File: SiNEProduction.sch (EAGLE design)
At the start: 35 parts, among them IC1 74HCT164D, IC3 ATTINY24/44/84-SSU, J1 AVR_SPI_PRG_6NS

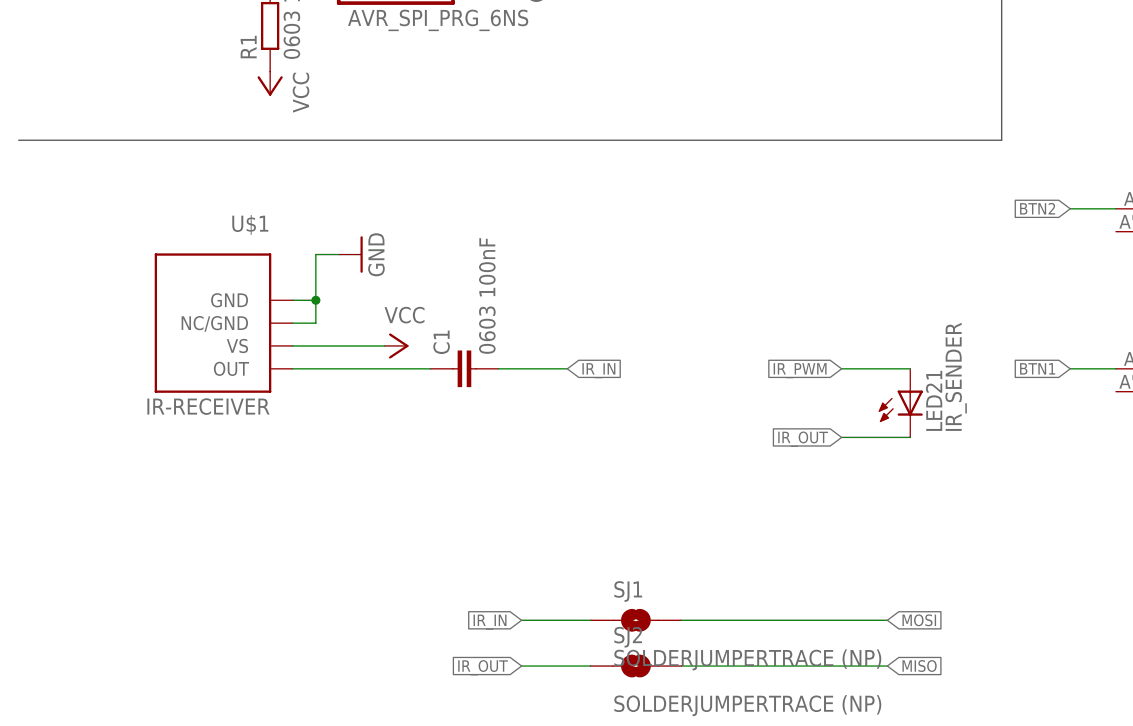
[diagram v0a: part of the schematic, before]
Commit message: Updated to use the combined IR Receiver footprint in case we have to switch parts
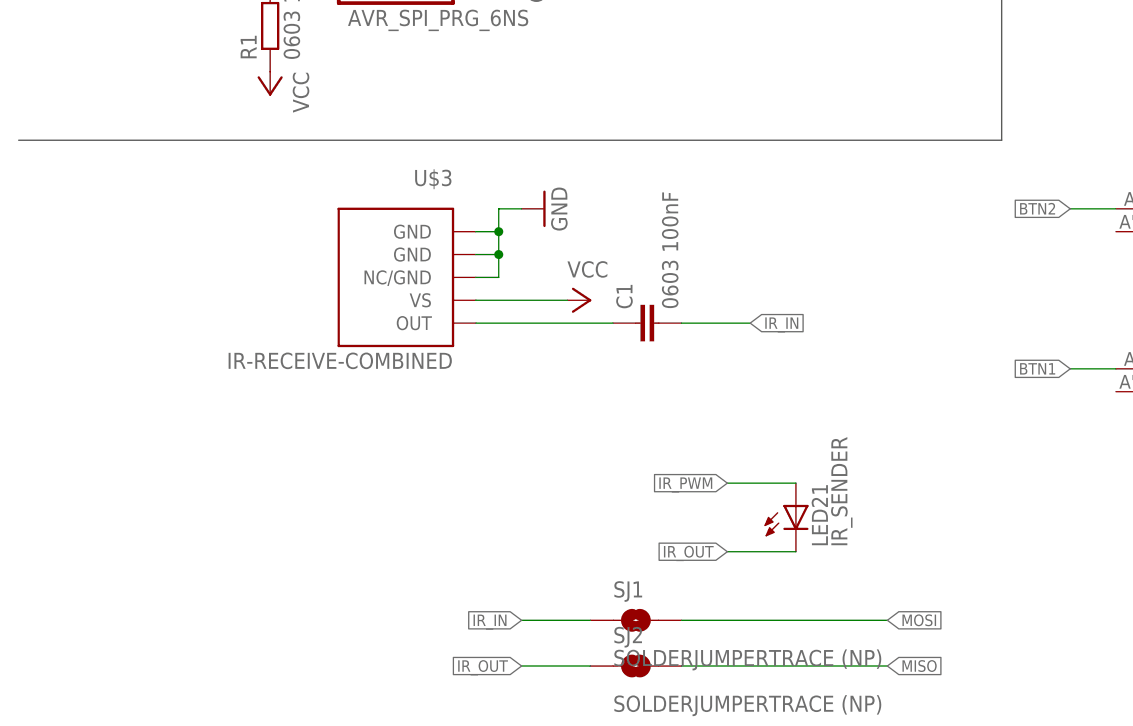
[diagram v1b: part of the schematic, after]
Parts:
- removed U$1: IR-RECEIVER, SiNE Parts:IR-RECEIVER
- added U$3: IR-RECEIVE-COMBINED, SiNE Parts:IR-RECEIVE-COMBINED
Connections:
- net GND: now also U$3.GND@1, U$3.GND@5, U$3.NC/GND@2; no longer U$1.GND, U$1.NC/GND
- net N$6: now also U$3.OUT@4; no longer U$1.OUT
- net VCC: now also U$3.VS@3; no longer U$1.VS
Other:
- moved on the sheet: C1, LED21
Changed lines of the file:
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@@
 <part name="SJ2" library="SparkFun" deviceset="SOLDERJUMPER" device="TRACE" value="SOLDERJUMPERTRACE (NP)"/>
 <part name="GND7" library="supply1" deviceset="GND" device=""/>
-<part name="U$1" library="SiNE Parts" deviceset="IR-RECEIVER" device=""/>
 <part name="IC3" library="SiNE Parts" deviceset="ATTINY24/44/84" device="-SSU"/>
 <part name="BAT2" library="SiNE Parts" deviceset="BATTERY" device="20SMD"/>
@@
 <part name="IC1" library="SiNE Parts" deviceset="74*164" device="D" technology="HCT"/>
 <part name="U$2" library="TiLDA" deviceset="MINIEMF" device=""/>
+<part name="U$3" library="SiNE Parts" deviceset="IR-RECEIVE-COMBINED" device=""/>
 </parts>
 <sheets>
@@
 <instance part="R2" gate="G$1" x="119.38" y="152.4" rot="R180"/>
 <instance part="P+5" gate="VCC" x="111.76" y="160.02"/>
-<instance part="P+6" gate="VCC" x="43.18" y="71.12" rot="R270"/>
-<instance part="C1" gate="G$1" x="48.26" y="68.58" rot="R90"/>
-<instance part="LED21" gate="G$1" x="99.06" y="66.04"/>
+<instance part="P+6" gate="VCC" x="63.5" y="76.2" rot="R270"/>
+<instance part="C1" gate="G$1" x="68.58" y="73.66" rot="R90"/>
+<instance part="LED21" gate="G$1" x="86.36" y="53.34"/>
 <instance part="B1" gate="G$1" x="127" y="68.58"/>
 <instance part="B2" gate="G$1" x="127" y="86.36"/>
@@
 <instance part="SJ1" gate="1" x="68.58" y="40.64"/>
 <instance part="SJ2" gate="1" x="68.58" y="35.56"/>
-<instance part="GND7" gate="1" x="38.1" y="81.28" rot="R90"/>
-<instance part="U$1" gate="G$1" x="22.86" y="73.66" rot="MR0"/>
+<instance part="GND7" gate="1" x="58.42" y="86.36" rot="R90"/>
 <instance part="IC3" gate="1" x="35.56" y="144.78"/>
 <instance part="BAT2" gate="G$1" x="86.36" y="114.3"/>
@@
 <instance part="IC1" gate="A" x="139.7" y="147.32"/>
 <instance part="U$2" gate="G$1" x="190.5" y="40.64"/>
+<instance part="U$3" gate="G$1" x="43.18" y="78.74" rot="MR0"/>
 </instances>
 <busses>
@@
 </segment>
 <segment>
-<wire x1="30.48" y1="73.66" x2="33.02" y2="73.66" width="0.1524" layer="91"/>
-<wire x1="33.02" y1="73.66" x2="33.02" y2="76.2" width="0.1524" layer="91"/>
-<wire x1="30.48" y1="76.2" x2="33.02" y2="76.2" width="0.1524" layer="91"/>
-<wire x1="33.02" y1="76.2" x2="33.02" y2="81.28" width="0.1524" layer="91"/>
-<wire x1="33.02" y1="81.28" x2="35.56" y2="81.28" width="0.1524" layer="91"/>
-<junction x="33.02" y="76.2"/>
+<wire x1="50.8" y1="78.74" x2="53.34" y2="78.74" width="0.1524" layer="91"/>
+<wire x1="53.34" y1="78.74" x2="53.34" y2="81.28" width="0.1524" layer="91"/>
+<wire x1="50.8" y1="81.28" x2="53.34" y2="81.28" width="0.1524" layer="91"/>
+<wire x1="53.34" y1="81.28" x2="53.34" y2="83.82" width="0.1524" layer="91"/>
+<wire x1="53.34" y1="83.82" x2="53.34" y2="86.36" width="0.1524" layer="91"/>
+<wire x1="53.34" y1="86.36" x2="55.88" y2="86.36" width="0.1524" layer="91"/>
+<junction x="53.34" y="81.28"/>
 <pinref part="GND7" gate="1" pin="GND"/>
-<pinref part="U$1" gate="G$1" pin="GND"/>
-<pinref part="U$1" gate="G$1" pin="NC/GND"/>
+<pinref part="U$3" gate="G$1" pin="GND@1"/>
+<pinref part="U$3" gate="G$1" pin="NC/GND@2"/>
+<pinref part="U$3" gate="G$1" pin="GND@5"/>
+<wire x1="50.8" y1="83.82" x2="53.34" y2="83.82" width="0.1524" layer="91"/>
+<junction x="53.34" y="83.82"/>
 </segment>
 </net>
@@
 <segment>
 <pinref part="P+6" gate="VCC" pin="VCC"/>
-<wire x1="40.64" y1="71.12" x2="30.48" y2="71.12" width="0.1524" layer="91"/>
-<pinref part="U$1" gate="G$1" pin="VS"/>
+<wire x1="60.96" y1="76.2" x2="50.8" y2="76.2" width="0.1524" layer="91"/>
+<pinref part="U$3" gate="G$1" pin="VS@3"/>
 </segment>
 </net>
@@
 <segment>
 <pinref part="C1" gate="G$1" pin="1"/>
-<wire x1="45.72" y1="68.58" x2="30.48" y2="68.58" width="0.1524" layer="91"/>
-<pinref part="U$1" gate="G$1" pin="OUT"/>
+<wire x1="66.04" y1="73.66" x2="50.8" y2="73.66" width="0.1524" layer="91"/>
+<pinref part="U$3" gate="G$1" pin="OUT@4"/>
 </segment>
 </net>
@@
 <segment>
 <pinref part="C1" gate="G$1" pin="2"/>
-<wire x1="53.34" y1="68.58" x2="60.96" y2="68.58" width="0.1524" layer="91"/>
-<label x="60.96" y="68.58" size="1.27" layer="95" font="vector" xref="yes"/>
+<wire x1="73.66" y1="73.66" x2="81.28" y2="73.66" width="0.1524" layer="91"/>
+<label x="81.28" y="73.66" size="1.27" layer="95" font="vector" xref="yes"/>
 </segment>
 <segment>
@@
 <segment>
 <pinref part="LED21" gate="G$1" pin="A"/>
-<wire x1="99.06" y1="68.58" x2="91.44" y2="68.58" width="0.1524" layer="91"/>
-<label x="91.44" y="68.58" size="1.27" layer="95" font="vector" rot="R180" xref="yes"/>
+<wire x1="86.36" y1="55.88" x2="78.74" y2="55.88" width="0.1524" layer="91"/>
+<label x="78.74" y="55.88" size="1.27" layer="95" font="vector" rot="R180" xref="yes"/>
 </segment>
 <segment>
@@
 <segment>
 <pinref part="LED21" gate="G$1" pin="C"/>
-<wire x1="99.06" y1="60.96" x2="91.44" y2="60.96" width="0.1524" layer="91"/>
-<label x="91.44" y="60.96" size="1.27" layer="95" font="vector" rot="R180" xref="yes"/>
-</segment>
-<segment>
+<wire x1="86.36" y1="48.26" x2="78.74" y2="48.26" width="0.1524" layer="91"/>
+<label x="78.74" y="48.26" size="1.27" layer="95" font="vector" rot="R180" xref="yes"/>
+</segment>
+<segment>

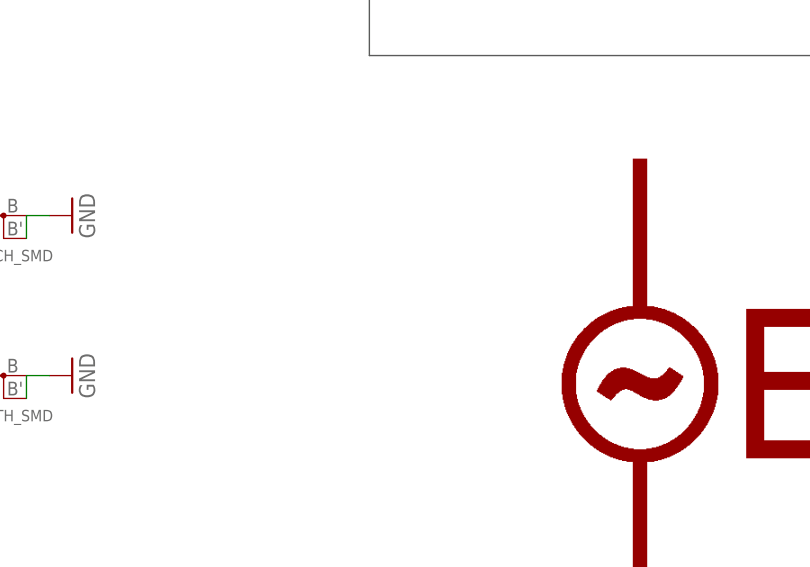
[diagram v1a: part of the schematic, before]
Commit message: Swapped sides for one button and IR Receiver Added bottom silk screen Added posible holle for Pin
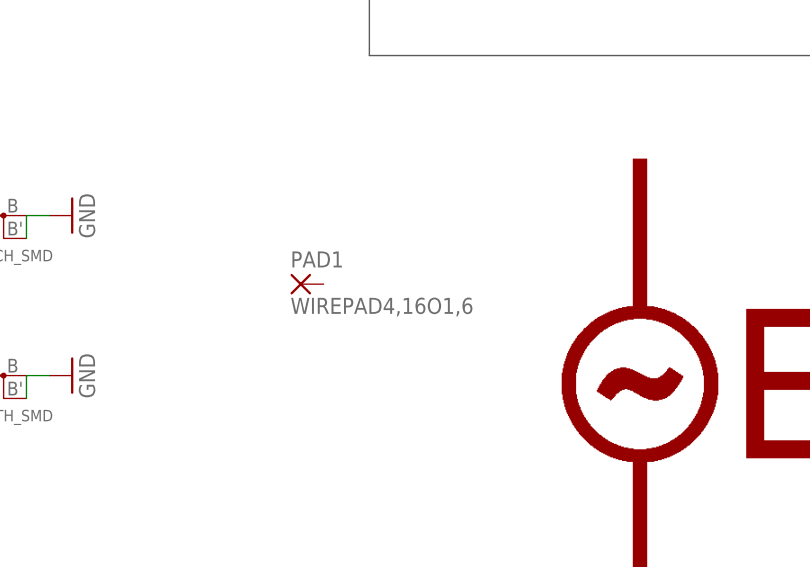
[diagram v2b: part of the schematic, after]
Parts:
- added PAD1: WIREPAD4,16O1,6, wirepad:WIREPAD4,16O1,6
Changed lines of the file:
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@@
 <grid distance="0.1" unitdist="inch" unit="inch" style="lines" multiple="1" display="no" altdistance="0.01" altunitdist="inch" altunit="inch"/>
 <layers>
-<layer number="1" name="Top" color="4" fill="1" visible="no" active="no"/>
-<layer number="2" name="Route2" color="1" fill="3" visible="no" active="no"/>
-<layer number="3" name="Route3" color="4" fill="3" visible="no" active="no"/>
-<layer number="4" name="Route4" color="1" fill="4" visible="no" active="no"/>
-<layer number="5" name="Route5" color="4" fill="4" visible="no" active="no"/>
-<layer number="6" name="Route6" color="1" fill="8" visible="no" active="no"/>
-<layer number="7" name="Route7" color="4" fill="8" visible="no" active="no"/>
-<layer number="8" name="Route8" color="1" fill="2" visible="no" active="no"/>
-<layer number="9" name="Route9" color="4" fill="2" visible="no" active="no"/>
-<layer number="10" name="Route10" color="1" fill="7" visible="no" active="no"/>
-<layer number="11" name="Route11" color="4" fill="7" visible="no" active="no"/>
-<layer number="12" name="Route12" color="1" fill="5" visible="no" active="no"/>
-<layer number="13" name="Route13" color="4" fill="5" visible="no" active="no"/>
-<layer number="14" name="Route14" color="1" fill="6" visible="no" active="no"/>
-<layer number="15" name="Route15" color="4" fill="6" visible="no" active="no"/>
-<layer number="16" name="Bottom" color="1" fill="1" visible="no" active="no"/>
-<layer number="17" name="Pads" color="2" fill="1" visible="no" active="no"/>
-<layer number="18" name="Vias" color="2" fill="1" visible="no" active="no"/>
-<layer number="19" name="Unrouted" color="6" fill="1" visible="no" active="no"/>
-<layer number="20" name="Dimension" color="15" fill="1" visible="no" active="no"/>
-<layer number="21" name="tPlace" color="7" fill="1" visible="no" active="no"/>
-<layer number="22" name="bPlace" color="7" fill="1" visible="no" active="no"/>
-<layer number="23" name="tOrigins" color="15" fill="1" visible="no" active="no"/>
-<layer number="24" name="bOrigins" color="15" fill="1" visible="no" active="no"/>
-<layer number="25" name="tNames" color="7" fill="1" visible="no" active="no"/>
-<layer number="26" name="bNames" color="7" fill="1" visible="no" active="no"/>
-<layer number="27" name="tValues" color="7" fill="1" visible="no" active="no"/>
-<layer number="28" name="bValues" color="7" fill="1" visible="no" active="no"/>
+<layer number="1" name="Top" color="4" fill="1" visible="yes" active="no"/>
+<layer number="2" name="Route2" color="1" fill="3" visible="yes" active="no"/>
+<layer number="3" name="Route3" color="4" fill="3" visible="yes" active="no"/>
+<layer number="4" name="Route4" color="1" fill="4" visible="yes" active="no"/>
+<layer number="5" name="Route5" color="4" fill="4" visible="yes" active="no"/>
+<layer number="6" name="Route6" color="1" fill="8" visible="yes" active="no"/>
+<layer number="7" name="Route7" color="4" fill="8" visible="yes" active="no"/>
+<layer number="8" name="Route8" color="1" fill="2" visible="yes" active="no"/>
+<layer number="9" name="Route9" color="4" fill="2" visible="yes" active="no"/>
+<layer number="10" name="Route10" color="1" fill="7" visible="yes" active="no"/>
+<layer number="11" name="Route11" color="4" fill="7" visible="yes" active="no"/>
+<layer number="12" name="Route12" color="1" fill="5" visible="yes" active="no"/>
+<layer number="13" name="Route13" color="4" fill="5" visible="yes" active="no"/>
+<layer number="14" name="Route14" color="1" fill="6" visible="yes" active="no"/>
+<layer number="15" name="Route15" color="4" fill="6" visible="yes" active="no"/>
+<layer number="16" name="Bottom" color="1" fill="1" visible="yes" active="no"/>
+<layer number="17" name="Pads" color="2" fill="1" visible="yes" active="no"/>
+<layer number="18" name="Vias" color="2" fill="1" visible="yes" active="no"/>
+<layer number="19" name="Unrouted" color="6" fill="1" visible="yes" active="no"/>
+<layer number="20" name="Dimension" color="15" fill="1" visible="yes" active="no"/>
+<layer number="21" name="tPlace" color="7" fill="1" visible="yes" active="no"/>
+<layer number="22" name="bPlace" color="7" fill="1" visible="yes" active="no"/>
+<layer number="23" name="tOrigins" color="15" fill="1" visible="yes" active="no"/>
+<layer number="24" name="bOrigins" color="15" fill="1" visible="yes" active="no"/>
+<layer number="25" name="tNames" color="7" fill="1" visible="yes" active="no"/>
+<layer number="26" name="bNames" color="7" fill="1" visible="yes" active="no"/>
+<layer number="27" name="tValues" color="7" fill="1" visible="yes" active="no"/>
+<layer number="28" name="bValues" color="7" fill="1" visible="yes" active="no"/>
 <layer number="29" name="tStop" color="7" fill="3" visible="no" active="no"/>
 <layer number="30" name="bStop" color="7" fill="6" visible="no" active="no"/>
@@
 <layer number="35" name="tGlue" color="7" fill="4" visible="no" active="no"/>
 <layer number="36" name="bGlue" color="7" fill="5" visible="no" active="no"/>
-<layer number="37" name="tTest" color="7" fill="1" visible="no" active="no"/>
-<layer number="38" name="bTest" color="7" fill="1" visible="no" active="no"/>
+<layer number="37" name="tTest" color="7" fill="1" visible="yes" active="no"/>
+<layer number="38" name="bTest" color="7" fill="1" visible="yes" active="no"/>
 <layer number="39" name="tKeepout" color="4" fill="11" visible="no" active="no"/>
 <layer number="40" name="bKeepout" color="1" fill="11" visible="no" active="no"/>
@@
 <layer number="44" name="Drills" color="7" fill="1" visible="no" active="no"/>
 <layer number="45" name="Holes" color="7" fill="1" visible="no" active="no"/>
-<layer number="46" name="Milling" color="3" fill="1" visible="no" active="no"/>
-<layer number="47" name="Measures" color="7" fill="1" visible="no" active="no"/>
-<layer number="48" name="Document" color="7" fill="1" visible="no" active="no"/>
-<layer number="49" name="Reference" color="7" fill="1" visible="no" active="no"/>
-<layer number="50" name="dxf" color="7" fill="1" visible="no" active="no"/>
-<layer number="51" name="tDocu" color="7" fill="1" visible="no" active="no"/>
-<layer number="52" name="bDocu" color="7" fill="1" visible="no" active="no"/>
-<layer number="53" name="tGND_GNDA" color="7" fill="9" visible="no" active="no"/>
-<layer number="54" name="bGND_GNDA" color="1" fill="9" visible="no" active="no"/>
-<layer number="56" name="wert" color="7" fill="1" visible="no" active="no"/>
+<layer number="46" name="Milling" color="3" fill="1" visible="yes" active="no"/>
+<layer number="47" name="Measures" color="7" fill="1" visible="yes" active="no"/>
+<layer number="48" name="Document" color="7" fill="1" visible="yes" active="no"/>
+<layer number="49" name="Reference" color="13" fill="1" visible="yes" active="no"/>
+<layer number="50" name="dxf" color="7" fill="1" visible="yes" active="no"/>
+<layer number="51" name="tDocu" color="14" fill="1" visible="yes" active="no"/>
+<layer number="52" name="bDocu" color="7" fill="1" visible="yes" active="no"/>
+<layer number="53" name="tGND_GNDA" color="7" fill="9" visible="yes" active="no"/>
+<layer number="54" name="bGND_GNDA" color="1" fill="9" visible="yes" active="no"/>
+<layer number="56" name="wert" color="7" fill="1" visible="yes" active="no"/>
 <layer number="91" name="Nets" color="2" fill="1" visible="yes" active="yes"/>
 <layer number="92" name="Busses" color="1" fill="1" visible="yes" active="yes"/>
@@
 <part name="U$2" library="TiLDA" deviceset="MINIEMF" device=""/>
 <part name="U$3" library="SiNE Parts" deviceset="IR-RECEIVE-COMBINED" device=""/>
+<part name="PAD1" library="wirepad" deviceset="WIREPAD" device="4,16O1,6"/>
 </parts>
 <sheets>
@@
 <instance part="U$2" gate="G$1" x="190.5" y="40.64"/>
 <instance part="U$3" gate="G$1" x="43.18" y="78.74" rot="MR0"/>
+<instance part="PAD1" gate="G$1" x="162.56" y="78.74"/>
 </instances>
 <busses>
